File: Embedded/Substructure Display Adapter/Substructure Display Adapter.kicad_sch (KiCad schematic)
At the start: 1 part, among them U1 D0 FFC

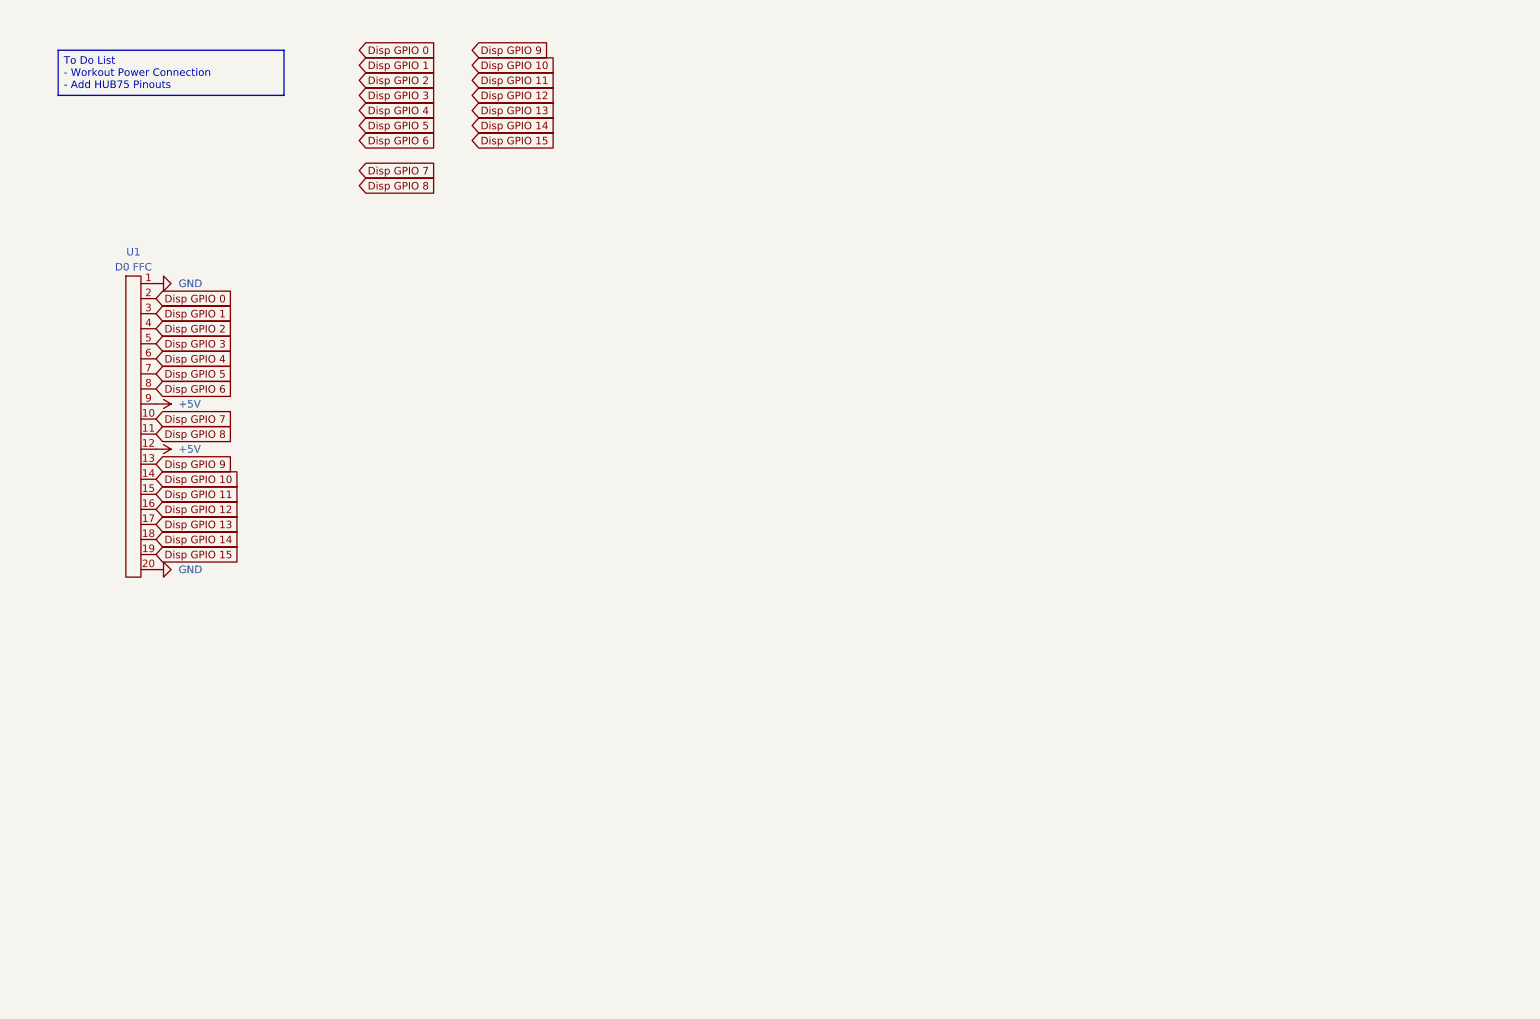
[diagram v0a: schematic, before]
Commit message: Added 3V3 to 5V Signal Level Shifter
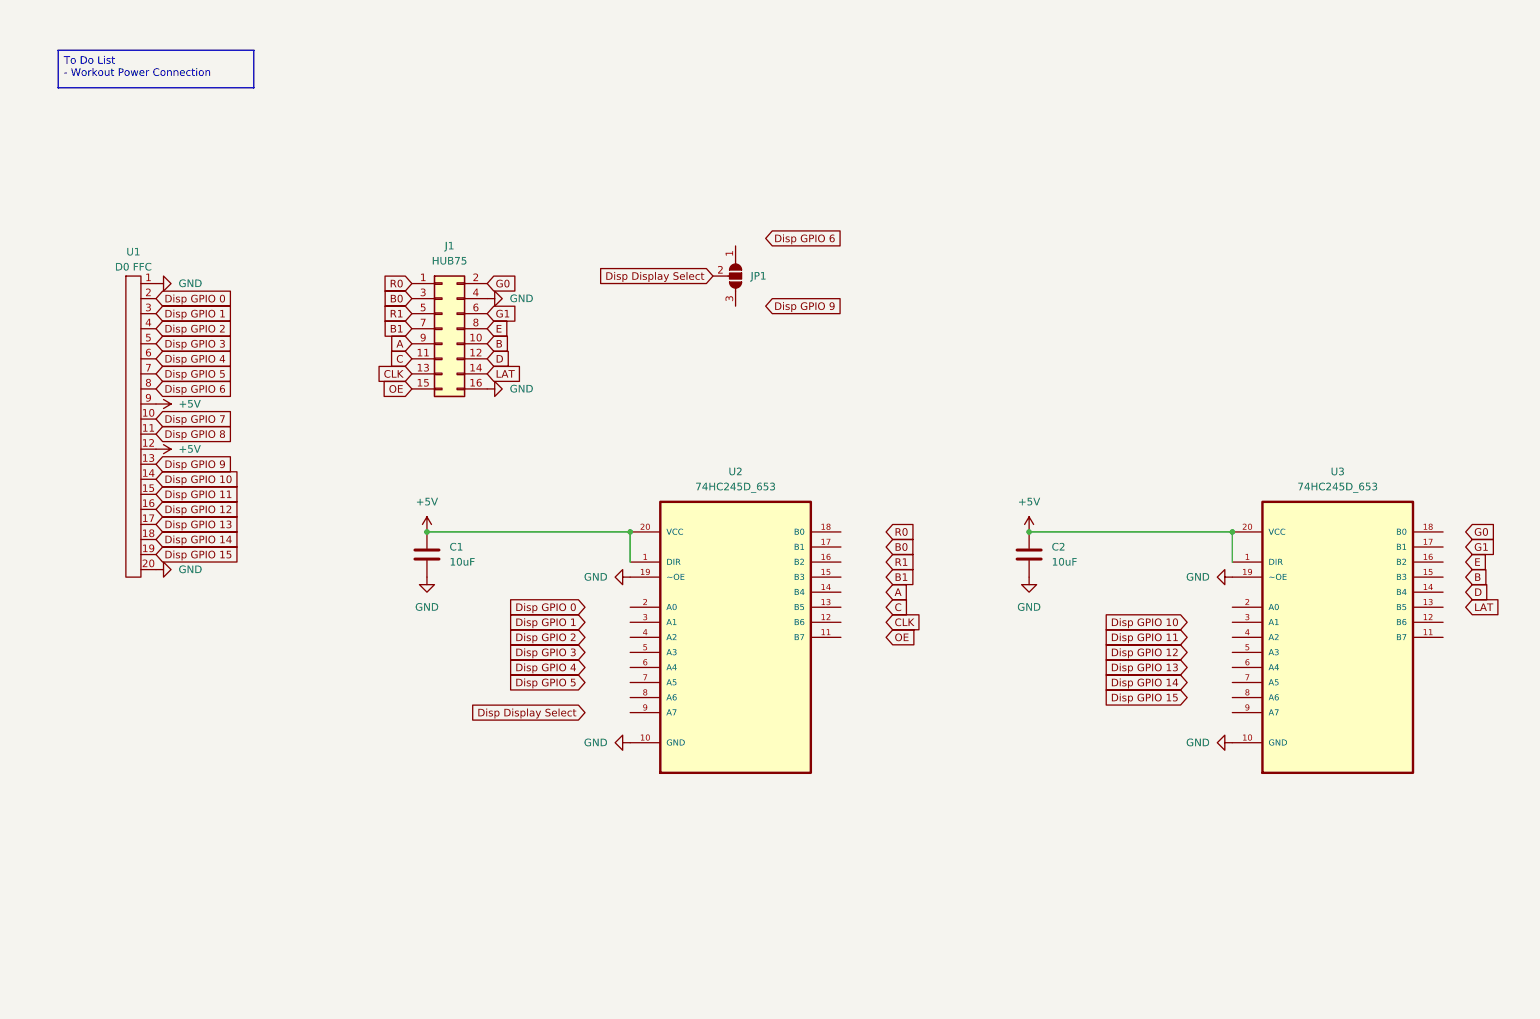
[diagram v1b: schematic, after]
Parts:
- added C1, C2: 10uF, symbol Device:C
- added J1: HUB75, Connector_PinHeader_2.54mm:PinHeader_2x08_P2.54mm_Vertical, symbol Connector_Generic:Conn_02x08_Odd_Even
- added JP1: SolderJumper_3_Open, Jumper:SolderJumper-3_P1.3mm_Open_RoundedPad1.0x1.5mm_NumberLabels, symbol Jumper:SolderJumper_3_Open
- added U2, U3: 74HC245D_653, 74HC245D:SOIC127P1032X265-20N, symbol 74HC245:74HC245D_653
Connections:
- net +5V: now also C1.1, C2.1, U2.1 (DIR), U2.20 (VCC), U3.1 (DIR), U3.20 (VCC)
- net GND: now also C1.2, C2.2, J1.16 (Pin_16), J1.4 (Pin_4), U2.10 (GND), U2.19 (~OE), U3.10 (GND), U3.19 (~OE)
- new net A: J1.9 (Pin_9)
- new net B: J1.10 (Pin_10)
- new net B0: J1.3 (Pin_3)
- new net B1: J1.7 (Pin_7)
- new net C: J1.11 (Pin_11)
- new net CLK: J1.13 (Pin_13)
- new net D: J1.12 (Pin_12)
- new net Disp Display Select: JP1.2 (C)
- new net E: J1.8 (Pin_8)
- new net G0: J1.2 (Pin_2)
- new net G1: J1.6 (Pin_6)
- new net LAT: J1.14 (Pin_14)
- new net OE: J1.15 (Pin_15)
- new net R0: J1.1 (Pin_1)
- new net R1: J1.5 (Pin_5)

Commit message: Added Power Ports
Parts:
- added J2: Input, Connector_JST:JST_XH_S4B-XH-A_1x04_P2.50mm_Horizontal, symbol Connector:Conn_01x04_Socket
- added J3: Output, Connector_JST:JST_VH_B4P-VH-B_1x04_P3.96mm_Vertical, symbol Connector_Generic:Conn_01x04
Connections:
- net +5V: now also J2.2 (Pin_2), J2.3 (Pin_3), J3.1 (Pin_1), J3.2 (Pin_2)
- net GND: now also J2.1 (Pin_1), J2.4 (Pin_4), J3.3 (Pin_3), J3.4 (Pin_4)

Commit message: Added PCB Component Placement
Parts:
- C1, C2: footprint (none) -> Capacitor_SMD:C_0603_1608Metric_Pad1.08x0.95mm_HandSolder
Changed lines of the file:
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@@
 			)
 		)
-		(property "Footprint" ""
+		(property "Footprint" "Capacitor_SMD:C_0603_1608Metric_Pad1.08x0.95mm_HandSolder"
 			(at 88.5952 114.3 0)
 			(effects
@@
 			)
 		)
-		(property "Footprint" ""
+		(property "Footprint" "Capacitor_SMD:C_0603_1608Metric_Pad1.08x0.95mm_HandSolder"
 			(at 190.1952 114.3 0)
 			(effects

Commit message: Added LCSC IDs
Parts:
- U2, U3: LCSC (none) -> C5625
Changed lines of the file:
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@@
+			)
+		)
+		(property "LCSC" "C5625"
+			(at 139.7 121.92 0)
+			(effects
+				(font
+					(size 1.27 1.27)
+				)
+				(hide yes)
 			)
 		)
@@
 				(hide yes)
 			)
+		)
+		(property "LCSC" "C5625"
+			(at 241.3 121.92 0)
+			(effects
+				(font
+					(size 1.27 1.27)
+				)
+				(hide yes)
+			)

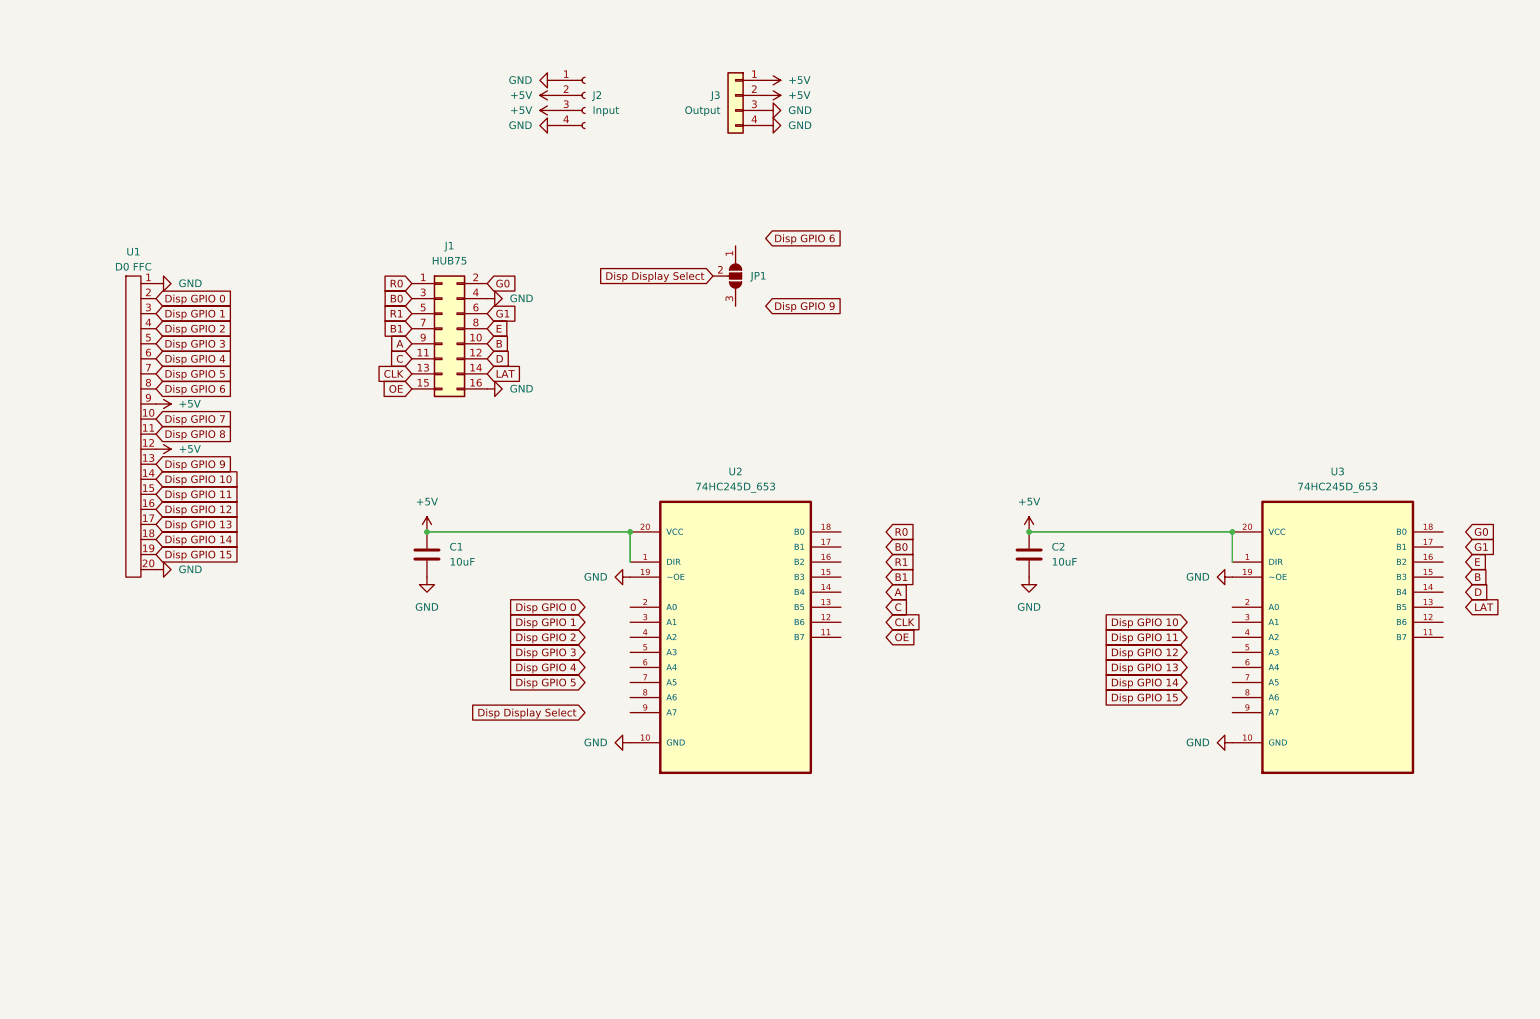
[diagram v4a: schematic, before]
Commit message: Added PCB Routing
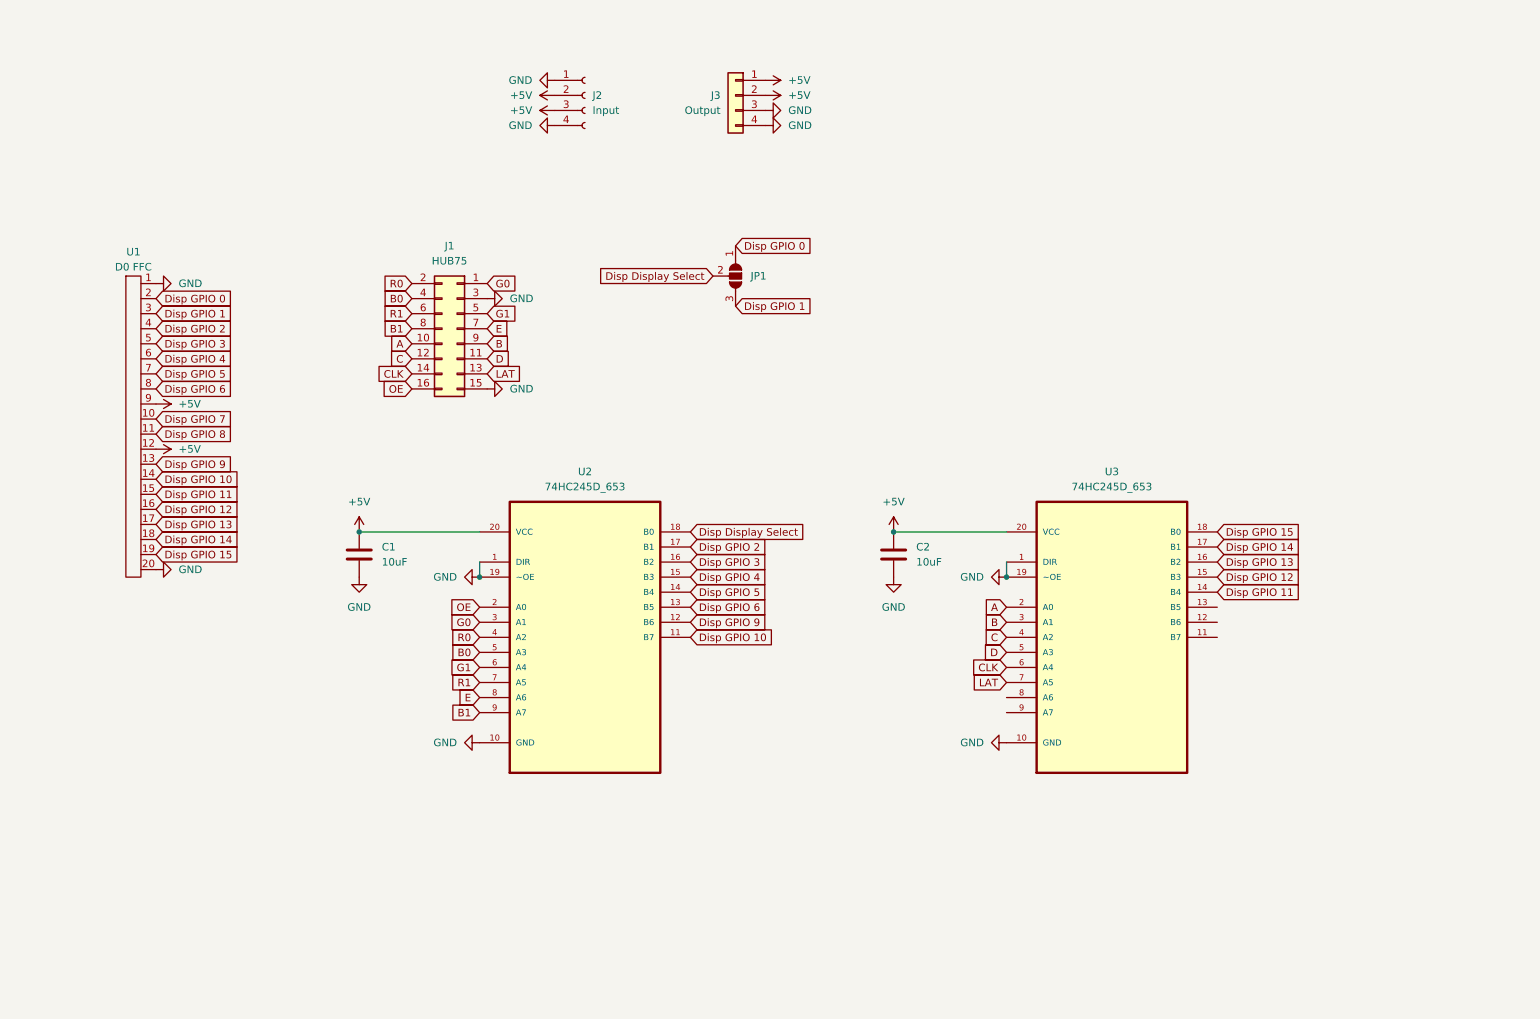
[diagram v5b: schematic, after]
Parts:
- C1, C2: LCSC (none) -> C95839
- J1: LCSC (none) -> C30734
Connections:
- net +5V: no longer U2.1 (DIR), U3.1 (DIR)
- net A: now also J1.10 (Pin_10), U3.2 (A0); no longer J1.9 (Pin_9)
- net B: now also J1.9 (Pin_9), U3.3 (A1); no longer J1.10 (Pin_10)
- net B0: now also J1.4 (Pin_4), U2.5 (A3); no longer J1.3 (Pin_3)
- net B1: now also J1.8 (Pin_8), U2.9 (A7); no longer J1.7 (Pin_7)
- net C: now also J1.12 (Pin_12), U3.4 (A2); no longer J1.11 (Pin_11)
- net CLK: now also J1.14 (Pin_14), U3.6 (A4); no longer J1.13 (Pin_13)
- net D: now also J1.11 (Pin_11), U3.5 (A3); no longer J1.12 (Pin_12)
- net Disp Display Select: now also U2.18 (B0)
- net Disp GPIO 0: now also JP1.1 (A)
- net Disp GPIO 1: now also JP1.3 (B)
- net Disp GPIO 10: now also U2.11 (B7)
- net Disp GPIO 11: now also U3.14 (B4)
- net Disp GPIO 12: now also U3.15 (B3)
- net Disp GPIO 13: now also U3.16 (B2)
- net Disp GPIO 14: now also U3.17 (B1)
- net Disp GPIO 15: now also U3.18 (B0)
- net Disp GPIO 2: now also U2.17 (B1)
- net Disp GPIO 3: now also U2.16 (B2)
- net Disp GPIO 4: now also U2.15 (B3)
- net Disp GPIO 5: now also U2.14 (B4)
- net Disp GPIO 6: now also U2.13 (B5)
- net Disp GPIO 9: now also U2.12 (B6)
- net E: now also J1.7 (Pin_7), U2.8 (A6); no longer J1.8 (Pin_8)
- net G0: now also J1.1 (Pin_1), U2.3 (A1); no longer J1.2 (Pin_2)
- net G1: now also J1.5 (Pin_5), U2.6 (A4); no longer J1.6 (Pin_6)
- net GND: now also J1.15 (Pin_15), J1.3 (Pin_3), U2.1 (DIR), U3.1 (DIR); no longer J1.16 (Pin_16), J1.4 (Pin_4)
- net LAT: now also J1.13 (Pin_13), U3.7 (A5); no longer J1.14 (Pin_14)
- net OE: now also J1.16 (Pin_16), U2.2 (A0); no longer J1.15 (Pin_15)
- net R0: now also J1.2 (Pin_2), U2.4 (A2); no longer J1.1 (Pin_1)
- net R1: now also J1.6 (Pin_6), U2.7 (A5); no longer J1.5 (Pin_5)
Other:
- moved on the sheet: C1, C2, U2, U3
